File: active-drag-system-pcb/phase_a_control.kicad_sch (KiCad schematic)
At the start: 18 parts, among them Q1 SIR182DP-T1-RE3, Q2 SIR182DP-T1-RE3, U11 IR2103, U12 INA180A3

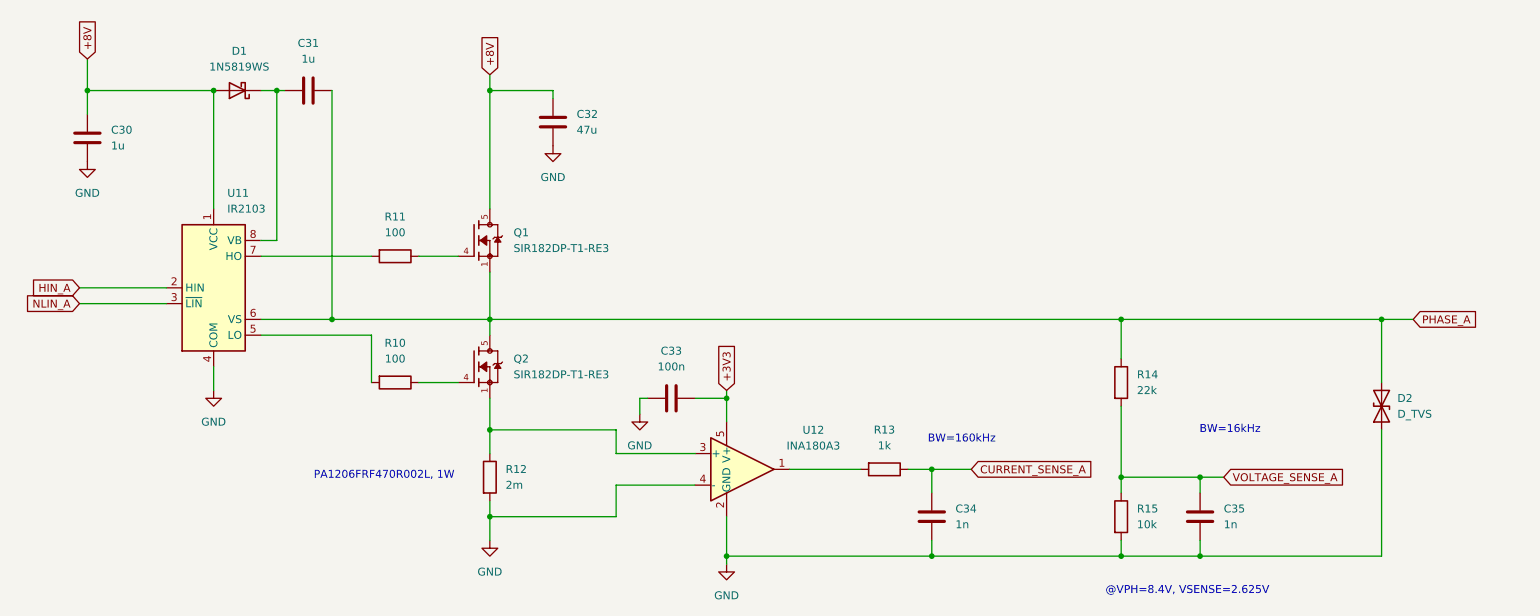
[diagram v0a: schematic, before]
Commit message: Swapped out regulators for higher current output; removed 8.4 V regulator; now two grounds (power and analog)
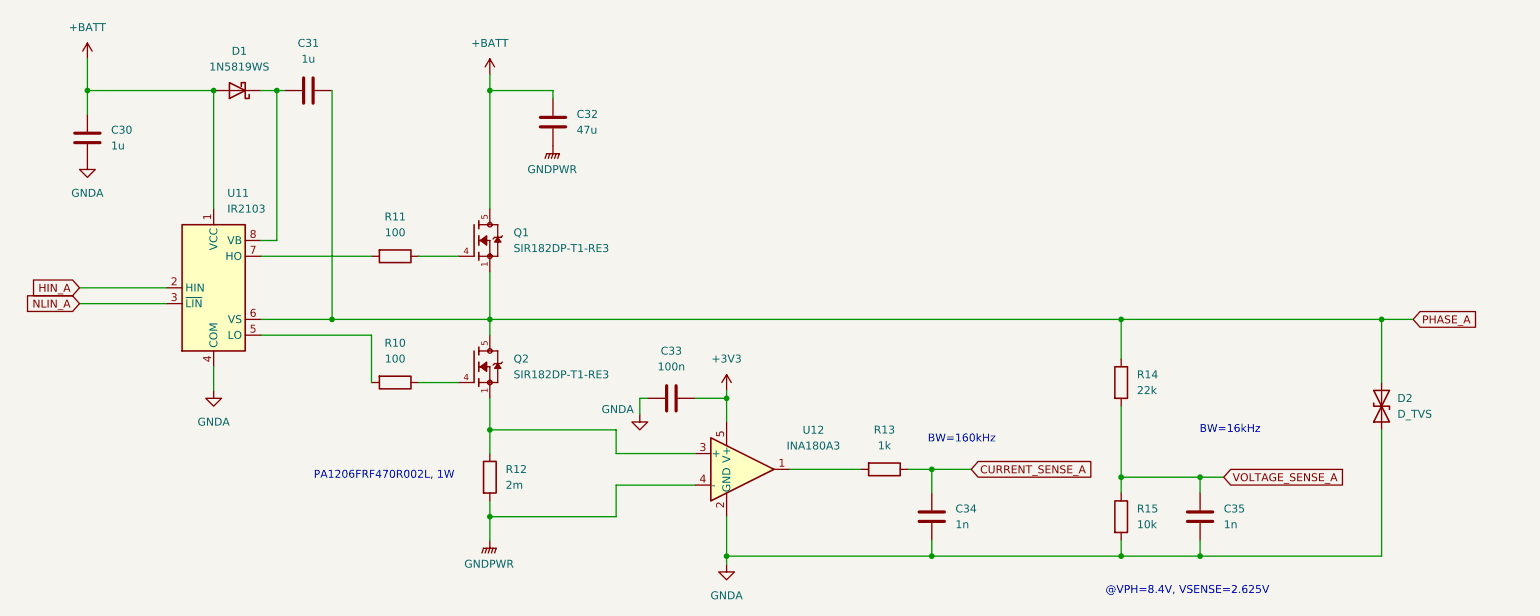
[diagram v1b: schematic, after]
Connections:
- net +8V renamed +BATT
- net GND renamed GNDA
- net GNDA: no longer C32.2, R12.2, U12.4 (-)
- new net GNDPWR: C32.2, R12.2, U12.4 (-)

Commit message: Literally everything has footprints and is pretty connected together on schematic except for IIM
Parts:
- removed C33: 100n, symbol Device:C
- removed C35: 1n, symbol Device:C
- removed D2: D_TVS, symbol Device:D_TVS
- added C28: 1uF, Capacitor_SMD:C_0402_1005Metric_Pad0.74x0.62mm_HandSolder, symbol Device:C
- added C29: 100n, Capacitor_SMD:C_0201_0603Metric_Pad0.64x0.40mm_HandSolder, symbol Device:C
- added D3: ESD131-B1-W0201, Diode_SMD:Infineon_SG-WLL-2-3_0.58x0.28_P0.36mm, symbol Diode:ESD131-B1-W0201
- C30: value 1u -> 1000pF; footprint (none) -> Capacitor_SMD:C_0402_1005Metric_Pad0.74x0.62mm_HandSolder; Dielectric (none) -> X7R; Max Voltage (none) -> 6.3V; Tolerance (none) -> 10%
- C31: value 1u -> 1uF; footprint (none) -> Capacitor_SMD:C_0402_1005Metric_Pad0.74x0.62mm_HandSolder; Dielectric (none) -> X5R; Max Voltage (none) -> 16V; Tolerance (none) -> 10%
- C32: footprint (none) -> Capacitor_SMD:C_1210_3225Metric_Pad1.33x2.70mm_HandSolder; Dielectric (none) -> X5R; Max Voltage (none) -> 16V; Tolerance (none) -> 20%
- C34: value 1n -> 1000pF; footprint (none) -> Capacitor_SMD:C_0402_1005Metric_Pad0.74x0.62mm_HandSolder; Dielectric (none) -> X7R; Max Voltage (none) -> 6.3V; Tolerance (none) -> 10%
- R10, R11: footprint (none) -> Resistor_SMD:R_2512_6332Metric_Pad1.40x3.35mm_HandSolder; Power (none) -> 1W; Tolerance (none) -> 5%
- R12: footprint (none) -> Resistor_SMD:R_1206_3216Metric_Pad1.30x1.75mm_HandSolder; Power (none) -> 1W; Tolerance (none) -> 1%
- R13: footprint (none) -> Resistor_SMD:R_0402_1005Metric_Pad0.72x0.64mm_HandSolder; Power (none) -> 0.1W; Tolerance (none) -> 1%
- R14: value 22k -> 39k; footprint (none) -> Resistor_SMD:R_0402_1005Metric_Pad0.72x0.64mm_HandSolder; Power (none) -> 0.1W; Tolerance (none) -> 5%
- R15: footprint (none) -> Resistor_SMD:R_0402_1005Metric_Pad0.72x0.64mm_HandSolder; Power (none) -> 0.1W; Tolerance (none) -> 5%
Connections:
- net +3V3: now also C29.2
- net +BATT: now also C28.1; no longer C30.1
- net GNDA: now also C28.2, C29.1, D3.1 (A1)
- net PHASE_A: now also D3.2 (A2)
- net VOLTAGE_SENSE_A: now also C30.1
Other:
- note added: "@VPH=12.6V, VSENSE=2.57V"
- note removed: "@VPH=8.4V, VSENSE=2.625V"

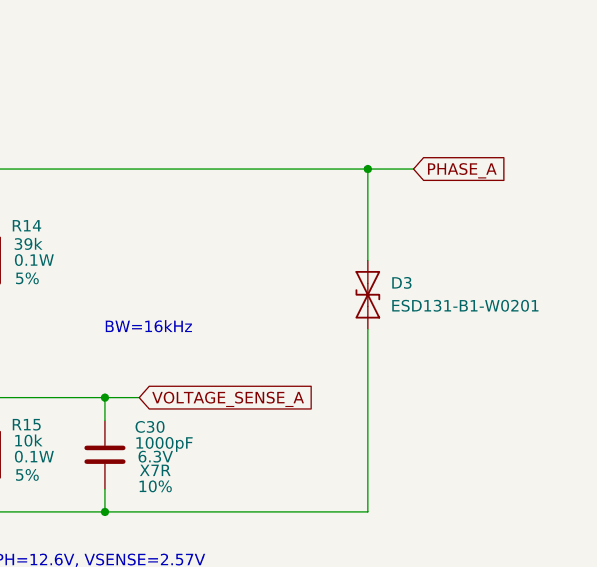
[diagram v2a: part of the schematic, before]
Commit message: Footprints for IIM; Disconnect AUX1 from GND, Leave as No-Connect
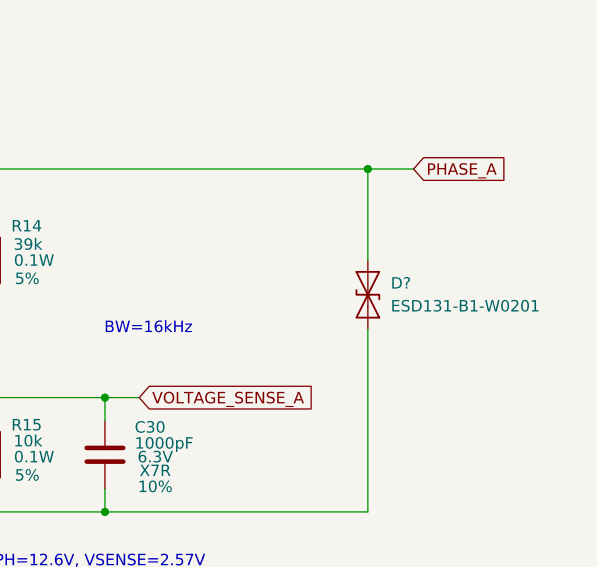
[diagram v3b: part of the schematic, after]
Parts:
- renumbered D3 to D?
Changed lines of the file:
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@@
 		(dnp no)
 		(fields_autoplaced yes)
-		(property "Reference" "#PWR016"
+		(property "Reference" "#PWR?"
 			(at 41.91 35.56 0)
 			(effects
@@
 		)
 		(pin "1"
+		)
+		(instances
+			(project "active-drag-system-pcb"
+				(path "/bbbb29dc-aa75-4226-931e-5c4f0b0fc0d6/fbbbaf64-191c-47c3-84ef-de04ddaa7763"
+					(reference "#PWR?")
+					(unit 1)
+				)
+			)
 		)
 	)
@@
 		(dnp no)
 		(fields_autoplaced yes)
-		(property "Reference" "#PWR025"
+		(property "Reference" "#PWR?"
 			(at 106.68 114.3 0)
 			(effects
@@
 		)
 		(pin "1"
+		)
+		(instances
+			(project "active-drag-system-pcb"
+				(path "/bbbb29dc-aa75-4226-931e-5c4f0b0fc0d6/fbbbaf64-191c-47c3-84ef-de04ddaa7763"
+					(reference "#PWR?")
+					(unit 1)
+				)
+			)
 		)
 	)
@@
 		(dnp no)
 		(fields_autoplaced yes)
-		(property "Reference" "#PWR030"
+		(property "Reference" "#PWR?"
 			(at 144.78 119.38 0)
 			(effects
@@
 		)
 		(pin "1"
+		)
+		(instances
+			(project "active-drag-system-pcb"
+				(path "/bbbb29dc-aa75-4226-931e-5c4f0b0fc0d6/fbbbaf64-191c-47c3-84ef-de04ddaa7763"
+					(reference "#PWR?")
+					(unit 1)
+				)
+			)
 		)
 	)
@@
 		(dnp no)
 		(fields_autoplaced yes)
-		(property "Reference" "#PWR029"
+		(property "Reference" "#PWR?"
 			(at 144.78 88.9 0)
 			(effects
@@
 		(pin "1"
 		)
+		(instances
+			(project "active-drag-system-pcb"
+				(path "/bbbb29dc-aa75-4226-931e-5c4f0b0fc0d6/fbbbaf64-191c-47c3-84ef-de04ddaa7763"
+					(reference "#PWR?")
+					(unit 1)
+				)
+			)
+		)
 	)
 	(symbol
@@
 		(dnp no)
 		(fields_autoplaced yes)
-		(property "Reference" "D3"
+		(property "Reference" "D?"
 			(at 252.73 86.3599 90)
 			(effects
@@
 		(pin "2"
 		)
-	)
+		(instances
+			(project "active-drag-system-pcb"
+				(path "/bbbb29dc-aa75-4226-931e-5c4f0b0fc0d6/fbbbaf64-191c-47c3-84ef-de04ddaa7763"
+					(reference "D?")
+					(unit 1)
+				)
+			)
+		)
+	)

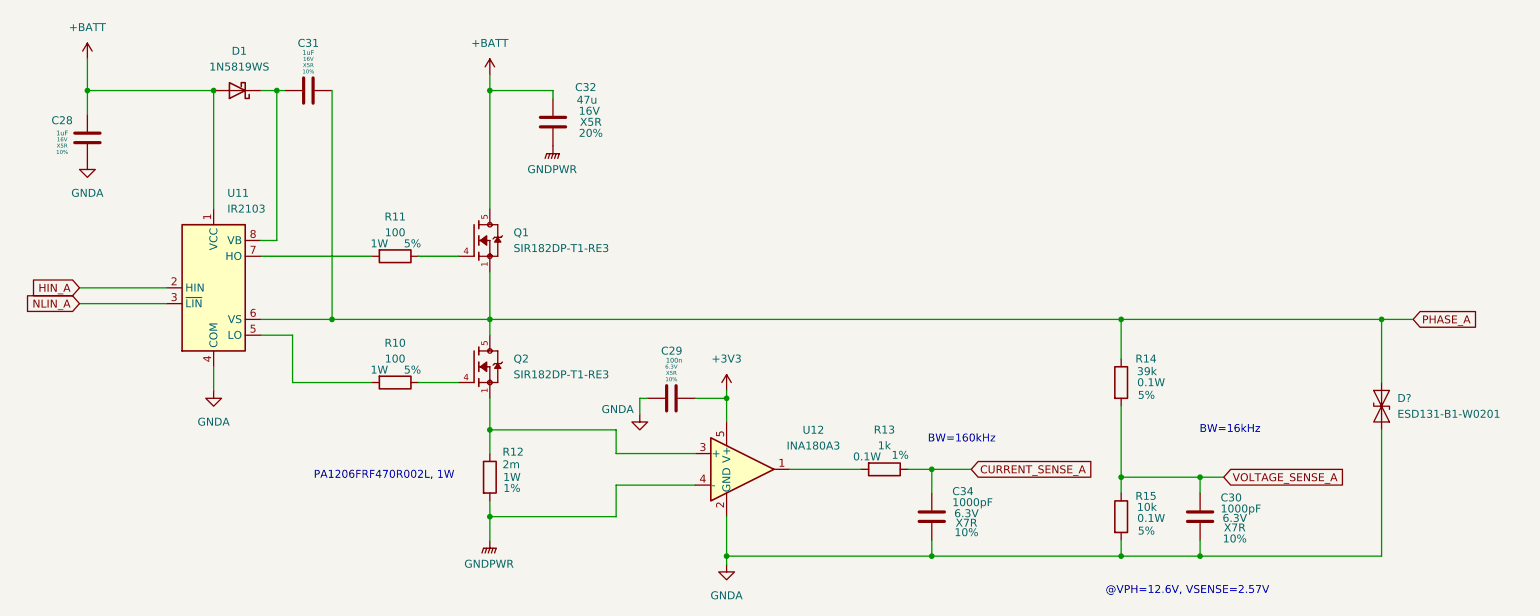
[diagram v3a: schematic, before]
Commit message: Updated Footprint library; Started component placement for 5V regulator
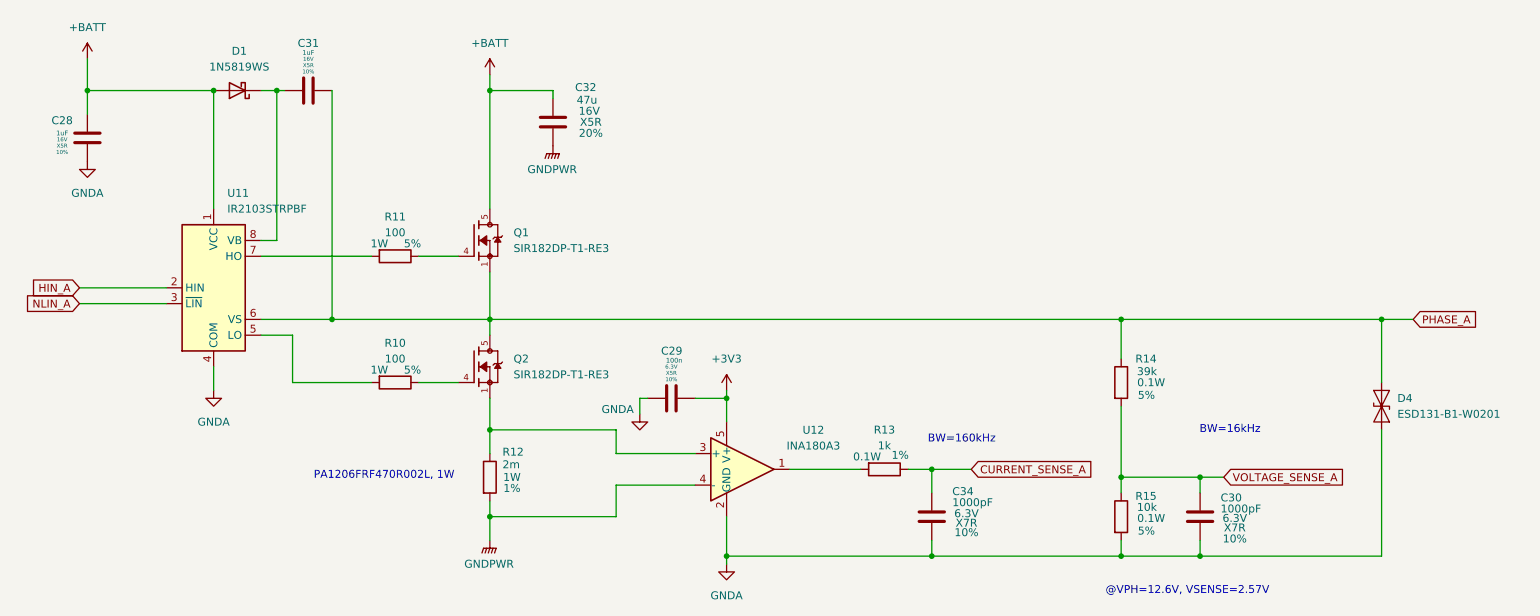
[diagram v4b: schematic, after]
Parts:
- removed D?: ESD131-B1-W0201, Diode_SMD:Infineon_SG-WLL-2-3_0.58x0.28_P0.36mm, symbol Diode:ESD131-B1-W0201
- added D4: ESD131-B1-W0201, Diode_SMD:Infineon_SG-WLL-2-3_0.58x0.28_P0.36mm, symbol Diode:ESD131-B1-W0201
- Q1, Q2: footprint SIR182DP-T1-RE3:TRANS_SIR182DP-T1-RE3 -> ADS_Library:TRANS_SIR182DP-T1-RE3
- U11: value IR2103 -> IR2103STRPBF; footprint (none) -> ADS_Library:SO8N_INF-L
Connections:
- net GNDA: now also D4.1 (A1)
- net PHASE_A: now also D4.2 (A2)
